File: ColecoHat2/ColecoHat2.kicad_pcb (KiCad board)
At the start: 2 copper layers, 56 x 65 mm, 7 parts, among them J1 CTRL1, J2 CTRL2, J3 PI_HEADER

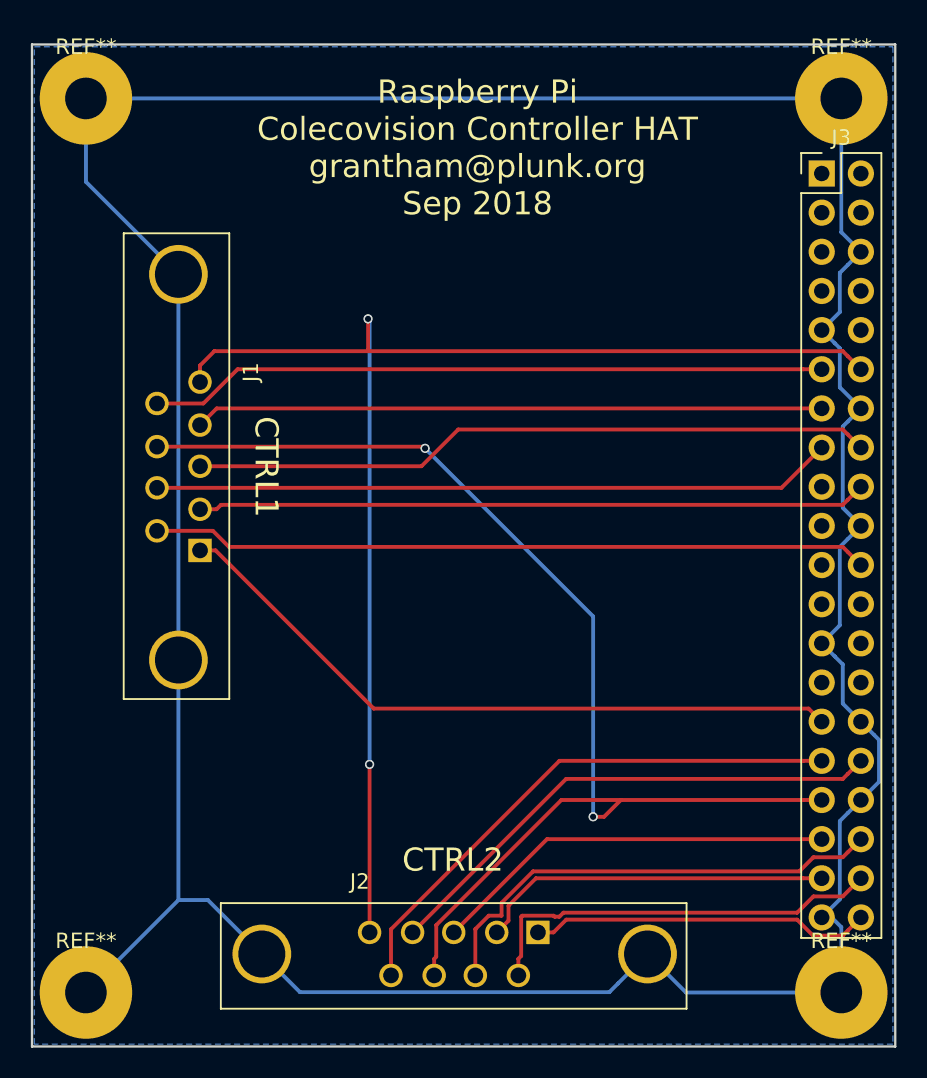
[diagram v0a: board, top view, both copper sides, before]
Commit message: update to PCB and BOM fields
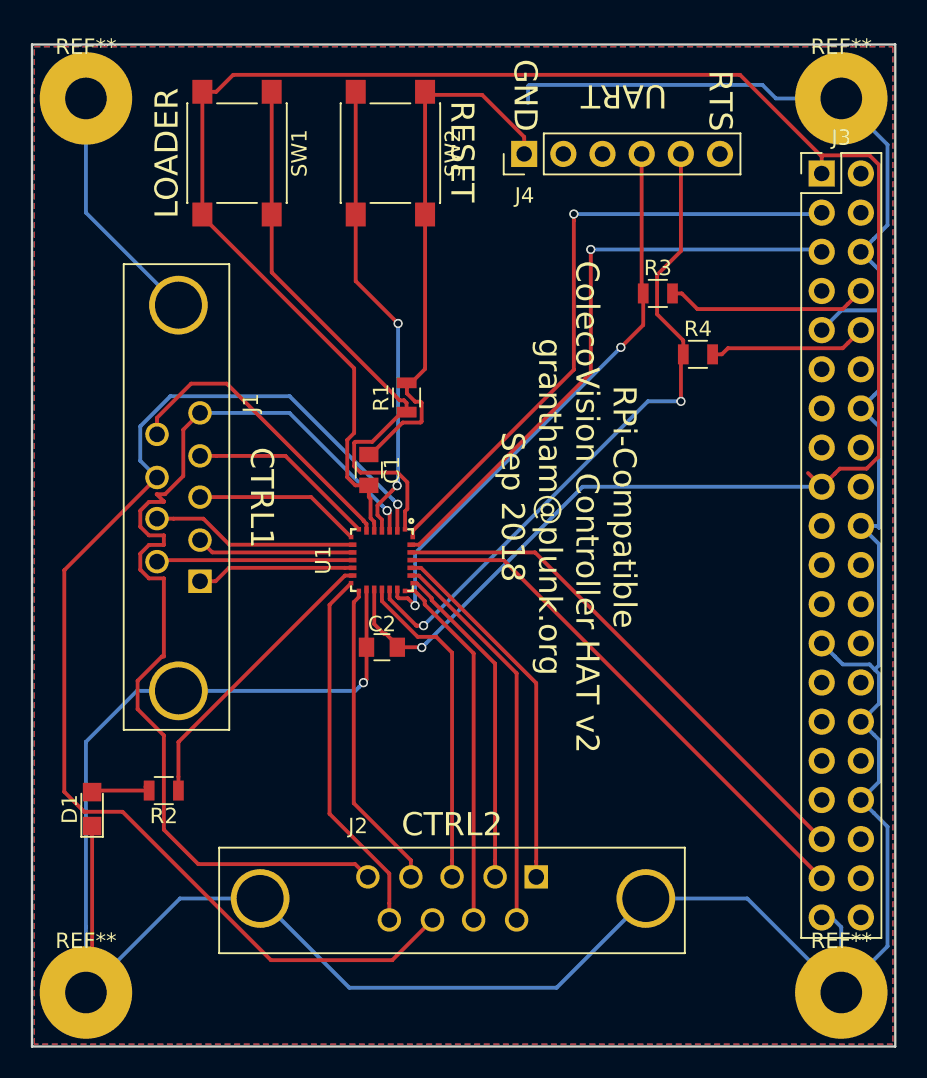
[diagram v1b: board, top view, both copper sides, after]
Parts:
- added C1: 100nF, Capacitors_SMD:C_0805, F.Cu at (149.3, 84.1)
- added C2: 100nF, Capacitors_SMD:C_0805, F.Cu at (150.2, 95.6)
- added D1: DEBUG LED, LEDs:LED_0805, F.Cu at (131.4, 106.1)
- added J4: CONN_01X06, Pin_Headers:Pin_Header_Straight_1x06_Pitch2.54mm, F.Cu at (159.4, 63.6)
- added R1: 10k, Resistors_SMD:R_0805, F.Cu at (151.8, 79.4)
- added R2: 220, Resistors_SMD:R_0805, F.Cu at (136.1, 104.9)
- added R3: 0, Resistors_SMD:R_0805, F.Cu at (168.1, 72.7)
- added R4: 0, Resistors_SMD:R_0805, F.Cu at (170.7, 76.6)
- added SW1: BOOTLOADER, Buttons_Switches_SMD:SW_SPST_PTS645, F.Cu at (140.8, 63.5)
- added SW2: RESET, Buttons_Switches_SMD:SW_SPST_PTS645, F.Cu at (150.8, 63.5)
- added U1: STM32L011G4U6, UFQFPN-28:UFQFPN-28, F.Cu at (150.2, 90.0)
- moved J2 3.60 mm to (160.2, 110.5)
- moved J1 2.00 mm to (138.4, 91.3)
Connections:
- J3 pad 1: Net-(J3-Pad1) -> +3V3
- J3 pad 11: QUADB1 -> Net-(J3-Pad11)
- J3 pad 12: SELECT_KEYPAD -> Net-(J3-Pad12)
- J3 pad 13: E1 -> Net-(J3-Pad13)
- J3 pad 15: QUADA1 -> Net-(J3-Pad15)
- J3 pad 16: W1 -> Net-(J3-Pad16)
- J3 pad 17: Net-(J3-Pad17) -> +3V3
- J3 pad 18: S1 -> Net-(J3-Pad18)
- J3 pad 22: FIRE1 -> Net-(J3-Pad22)
- J3 pad 29: N1 -> Net-(J3-Pad29)
- J3 pad 3: Net-(J3-Pad3) -> I2C1_SDA
- J3 pad 31: QUADB2 -> Net-(J3-Pad31)
- J3 pad 32: E2 -> Net-(J3-Pad32)
- J3 pad 33: SELECT_JOYSTICK -> Net-(J3-Pad33)
- J3 pad 35: W2 -> IRQ
- J3 pad 36: QUADA2 -> Net-(J3-Pad36)
- J3 pad 37: S2 -> DEBUG_GPIO
- J3 pad 38: FIRE2 -> Net-(J3-Pad38)
- J3 pad 40: N2 -> Net-(J3-Pad40)
- J3 pad 5: Net-(J3-Pad5) -> I2C1_SCL
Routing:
- net +3V3: track 0.00 -> 142.9 mm, vias 0 -> 1
- net USART1_TX: track 0.00 -> 43.7 mm, vias 0 -> 2
- net I2C1_SDA: track 0.00 -> 41.4 mm, vias 0 -> 1
- net GND: track 226.1 -> 266.1 mm, vias 0 -> 1
- net I2C1_SCL: track 0.00 -> 39.3 mm, vias 0 -> 1
- net USART1_RX: track 0.00 -> 37.3 mm, vias 0 -> 2
- net BOOTLOADER: track 0.00 -> 37.3 mm
- net DEBUG_GPIO: track 0.00 -> 35.2 mm
- net N1: track 44.9 -> 10.3 mm
- net IRQ: track 0.00 -> 34.3 mm
- net FIRE1: track 46.6 -> 12.7 mm
- net W1: track 44.3 -> 10.9 mm
- net S1: track 43.5 -> 10.2 mm
- net QUADA1: track 44.2 -> 13.4 mm
- net Net-(SW2-Pad2): track 0.00 -> 30.1 mm, vias 0 -> 2
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- added copper zone on F.Cu, net +3V3
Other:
- board text added: "GND"
- board text added: "LOADER"
- board text added: "RESET"
- board text added: "RPi-Compatible ColecoVision Controller HAT v2 grantham@plunk.org Sep 2018"
- board text added: "RTS"
- board text added: "UART"
- board text removed: "Raspberry Pi Colecovision Controller HAT grantham@plunk.org Sep 2018"

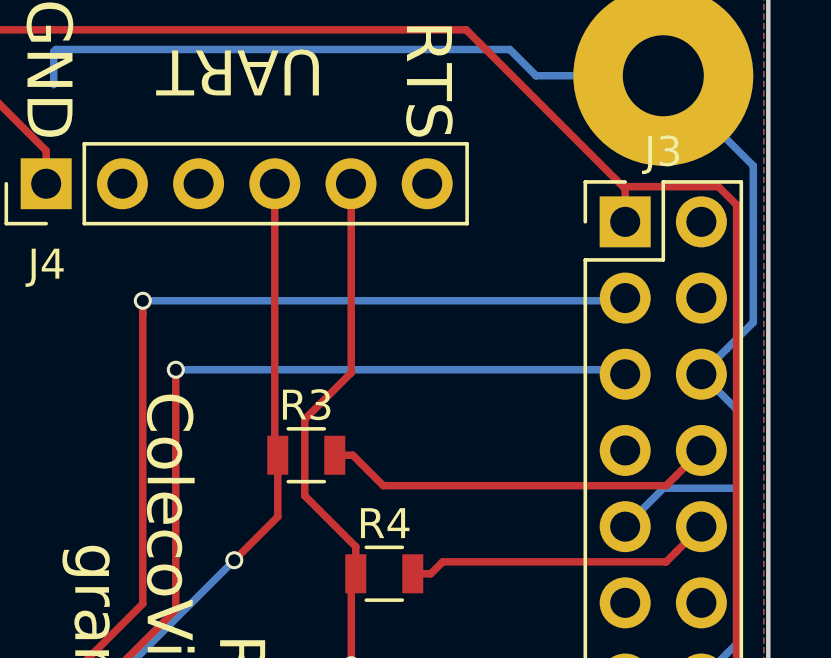
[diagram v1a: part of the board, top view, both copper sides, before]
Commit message: add pull-ups for UART
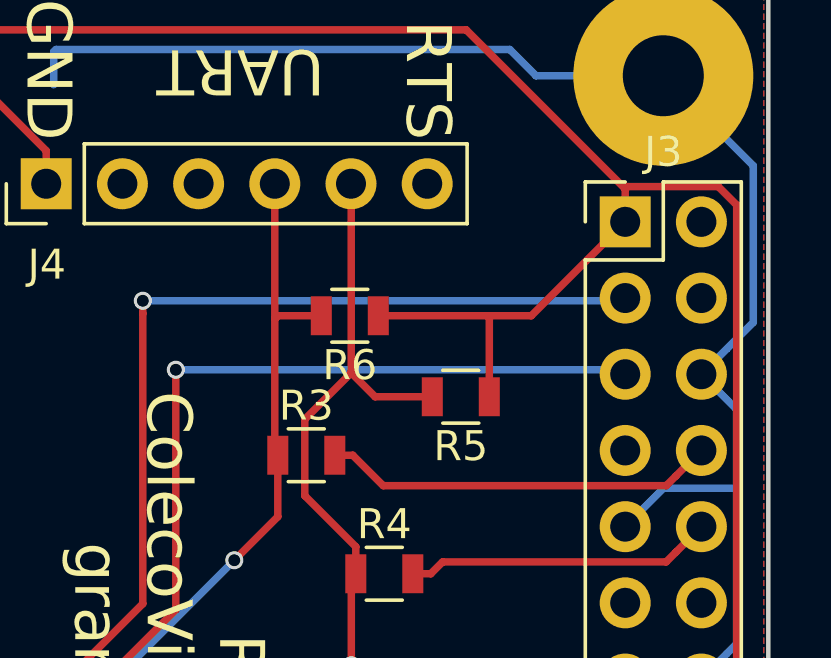
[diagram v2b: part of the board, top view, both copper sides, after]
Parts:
- added R5: 100k, Resistors_SMD:R_0805, F.Cu at (173.2, 70.7)
- added R6: 100k, Resistors_SMD:R_0805, F.Cu at (169.6, 68.0)
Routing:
- net +3V3: track 142.9 -> 156.0 mm
- net USART1_TX: track 43.7 -> 46.8 mm
- net USART1_RX: track 37.3 -> 38.9 mm
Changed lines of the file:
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@@
 (kicad_pcb (version 4) (host pcbnew 4.0.6)
   (general
-    (links 65)
+    (links 69)
     (no_connects 0)
-    (area 115.871429 55.675 195.128572 122.425)
+    (area 127.424999 56.424999 183.575001 121.575001)
     (thickness 1.6)
     (drawings 12)
-    (tracks 318)
+    (tracks 328)
     (zones 0)
-    (modules 18)
+    (modules 20)
     (nets 58)
   )
@@
     (visible_elements FFFFFF7F)
     (pcbplotparams
-      (layerselection 0x010f0_80000001)
+      (layerselection 0x310fc_80000001)
       (usegerberextensions true)
       (excludeedgelayer true)
@@
       (net 10 QUADB1))
     (model ${KISYS3DMOD}/Connectors.3dshapes/DB9FD.wrl
-      (at (xyz -0.2086614173228347 -0.05118110236220473 0))
+      (at (xyz -0.208661 -0.051181 0))
       (scale (xyz 1 1 1))
       (rotate (xyz 0 0 0))
@@
       (net 17 QUADB2))
     (model ${KISYS3DMOD}/Connectors.3dshapes/DB9FD.wrl
-      (at (xyz -0.2086614173228347 -0.05118110236220473 0))
+      (at (xyz -0.208661 -0.051181 0))
       (scale (xyz 1 1 1))
       (rotate (xyz 0 0 0))
@@
   (module UFQFPN-28:UFQFPN-28 (layer F.Cu)
     (at 150.2 89.95 270)
+    (attr smd)
     (fp_text reference U1 (at 0 3.81 270) (layer F.SilkS)
       (effects (font (size 1 1) (thickness 0.15)))
@@
       (scale (xyz 1 1 1))
       (rotate (xyz 0 0 180))
+    )
+  )
+  (module Resistors_SMD:R_0805 (layer F.Cu)
+    (at 173.25 70.7 180)
+    (descr "Resistor SMD 0805, reflow soldering, Vishay (see dcrcw.pdf)")
+    (tags "resistor 0805")
+    (attr smd)
+    (fp_text reference R5 (at 0 -1.65 180) (layer F.SilkS)
+      (effects (font (size 1 1) (thickness 0.15)))
+    )
+    (fp_text value 100k (at 0 1.75 180) (layer F.Fab)
+      (effects (font (size 1 1) (thickness 0.15)))
+    )
+    (fp_text user %R (at 0 0 180) (layer F.Fab)
+      (effects (font (size 0.5 0.5) (thickness 0.075)))
+    )
+    (fp_line (start -1 0.62) (end -1 -0.62) (layer F.Fab) (width 0.1))
+    (fp_line (start 1 0.62) (end -1 0.62) (layer F.Fab) (width 0.1))
+    (fp_line (start 1 -0.62) (end 1 0.62) (layer F.Fab) (width 0.1))
+    (fp_line (start -1 -0.62) (end 1 -0.62) (layer F.Fab) (width 0.1))
+    (fp_line (start 0.6 0.88) (end -0.6 0.88) (layer F.SilkS) (width 0.12))
+    (fp_line (start -0.6 -0.88) (end 0.6 -0.88) (layer F.SilkS) (width 0.12))
+    (fp_line (start -1.55 -0.9) (end 1.55 -0.9) (layer F.CrtYd) (width 0.05))
+    (fp_line (start -1.55 -0.9) (end -1.55 0.9) (layer F.CrtYd) (width 0.05))
+    (fp_line (start 1.55 0.9) (end 1.55 -0.9) (layer F.CrtYd) (width 0.05))
+    (fp_line (start 1.55 0.9) (end -1.55 0.9) (layer F.CrtYd) (width 0.05))
+    (pad 1 smd rect (at -0.95 0 180) (size 0.7 1.3) (layers F.Cu F.Paste F.Mask)
+      (net 30 +3V3))
+    (pad 2 smd rect (at 0.95 0 180) (size 0.7 1.3) (layers F.Cu F.Paste F.Mask)
+      (net 52 USART1_TX))
+    (model ${KISYS3DMOD}/Resistors_SMD.3dshapes/R_0805.wrl
+      (at (xyz 0 0 0))
+      (scale (xyz 1 1 1))
+      (rotate (xyz 0 0 0))
+    )
+  )
+  (module Resistors_SMD:R_0805 (layer F.Cu)
+    (at 169.55 68 180)
+    (descr "Resistor SMD 0805, reflow soldering, Vishay (see dcrcw.pdf)")
+    (tags "resistor 0805")
+    (attr smd)
+    (fp_text reference R6 (at 0 -1.65 180) (layer F.SilkS)
+      (effects (font (size 1 1) (thickness 0.15)))
+    )
+    (fp_text value 100k (at 0 1.75 180) (layer F.Fab)
+      (effects (font (size 1 1) (thickness 0.15)))
+    )
+    (fp_text user %R (at 0 0 180) (layer F.Fab)
+      (effects (font (size 0.5 0.5) (thickness 0.075)))
+    )
+    (fp_line (start -1 0.62) (end -1 -0.62) (layer F.Fab) (width 0.1))
+    (fp_line (start 1 0.62) (end -1 0.62) (layer F.Fab) (width 0.1))
+    (fp_line (start 1 -0.62) (end 1 0.62) (layer F.Fab) (width 0.1))
+    (fp_line (start -1 -0.62) (end 1 -0.62) (layer F.Fab) (width 0.1))
+    (fp_line (start 0.6 0.88) (end -0.6 0.88) (layer F.SilkS) (width 0.12))
+    (fp_line (start -0.6 -0.88) (end 0.6 -0.88) (layer F.SilkS) (width 0.12))
+    (fp_line (start -1.55 -0.9) (end 1.55 -0.9) (layer F.CrtYd) (width 0.05))
+    (fp_line (start -1.55 -0.9) (end -1.55 0.9) (layer F.CrtYd) (width 0.05))
+    (fp_line (start 1.55 0.9) (end 1.55 -0.9) (layer F.CrtYd) (width 0.05))
+    (fp_line (start 1.55 0.9) (end -1.55 0.9) (layer F.CrtYd) (width 0.05))
+    (pad 1 smd rect (at -0.95 0 180) (size 0.7 1.3) (layers F.Cu F.Paste F.Mask)
+      (net 30 +3V3))
+    (pad 2 smd rect (at 0.95 0 180) (size 0.7 1.3) (layers F.Cu F.Paste F.Mask)
+      (net 51 USART1_RX))
+    (model ${KISYS3DMOD}/Resistors_SMD.3dshapes/R_0805.wrl
+      (at (xyz 0 0 0))
+      (scale (xyz 1 1 1))
+      (rotate (xyz 0 0 0))
     )
   )
@@
   (segment (start 172.25 76.6) (end 172.644999 76.205001) (width 0.25) (layer F.Cu) (net 22))
   (segment (start 172.644999 76.205001) (end 180.094999 76.205001) (width 0.25) (layer F.Cu) (net 22))
+  (segment (start 170.5 68) (end 174.2 68) (width 0.25) (layer F.Cu) (net 30))
+  (segment (start 174.2 68) (end 175.6 68) (width 0.25) (layer F.Cu) (net 30))
+  (segment (start 174.2 70.7) (end 174.2 68) (width 0.25) (layer F.Cu) (net 30))
+  (segment (start 175.6 68) (end 178.73 64.87) (width 0.25) (layer F.Cu) (net 30))
+  (segment (start 178.1 65.5) (end 178.73 64.87) (width 0.25) (layer F.Cu) (net 30))
   (segment (start 138.55 59.57) (end 139.45 59.57) (width 0.25) (layer F.Cu) (net 30))
   (segment (start 140.550001 58.469999) (end 173.429999 58.469999) (width 0.25) (layer F.Cu) (net 30))
@@
   (segment (start 131.5 104.9) (end 131.4 105) (width 0.25) (layer F.Cu) (net 50))
   (segment (start 134.85 104.65) (end 135.1 104.9) (width 0.25) (layer F.Cu) (net 50))
-  (segment (start 167.05 63.6) (end 167.05 72.55) (width 0.25) (layer F.Cu) (net 51))
+  (segment (start 167.05 63.6) (end 167.05 68.1) (width 0.25) (layer F.Cu) (net 51))
+  (segment (start 167.05 68.1) (end 167.05 72.55) (width 0.25) (layer F.Cu) (net 51))
+  (segment (start 168.6 68) (end 167.15 68) (width 0.25) (layer F.Cu) (net 51))
+  (segment (start 167.15 68) (end 167.05 68.1) (width 0.25) (layer F.Cu) (net 51))
   (segment (start 167.05 72.55) (end 167.15 72.65) (width 0.25) (layer F.Cu) (net 51))
   (segment (start 152.35 92.9) (end 151.875001 92.425001) (width 0.25) (layer F.Cu) (net 51))
@@
   (segment (start 167.15 74.7) (end 165.7 76.15) (width 0.25) (layer F.Cu) (net 51))
   (via (at 165.7 76.15) (size 0.6) (drill 0.4) (layers F.Cu B.Cu) (net 51))
+  (segment (start 172.3 70.7) (end 170.39447 70.7) (width 0.25) (layer F.Cu) (net 52))
+  (segment (start 170.39447 70.7) (end 169.597235 69.902765) (width 0.25) (layer F.Cu) (net 52))
   (segment (start 169.59 63.6) (end 169.597235 63.607235) (width 0.25) (layer F.Cu) (net 52))
   (segment (start 169.597235 63.607235) (end 169.597235 69.902765) (width 0.25) (layer F.Cu) (net 52))
